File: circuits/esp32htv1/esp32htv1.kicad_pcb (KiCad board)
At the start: 2 copper layers, 56.6 x 57.7 mm, 8 parts, among them U1 BME280, U2 ESP32-WROOM-32UE, U3 LD1117S33TR_SOT223

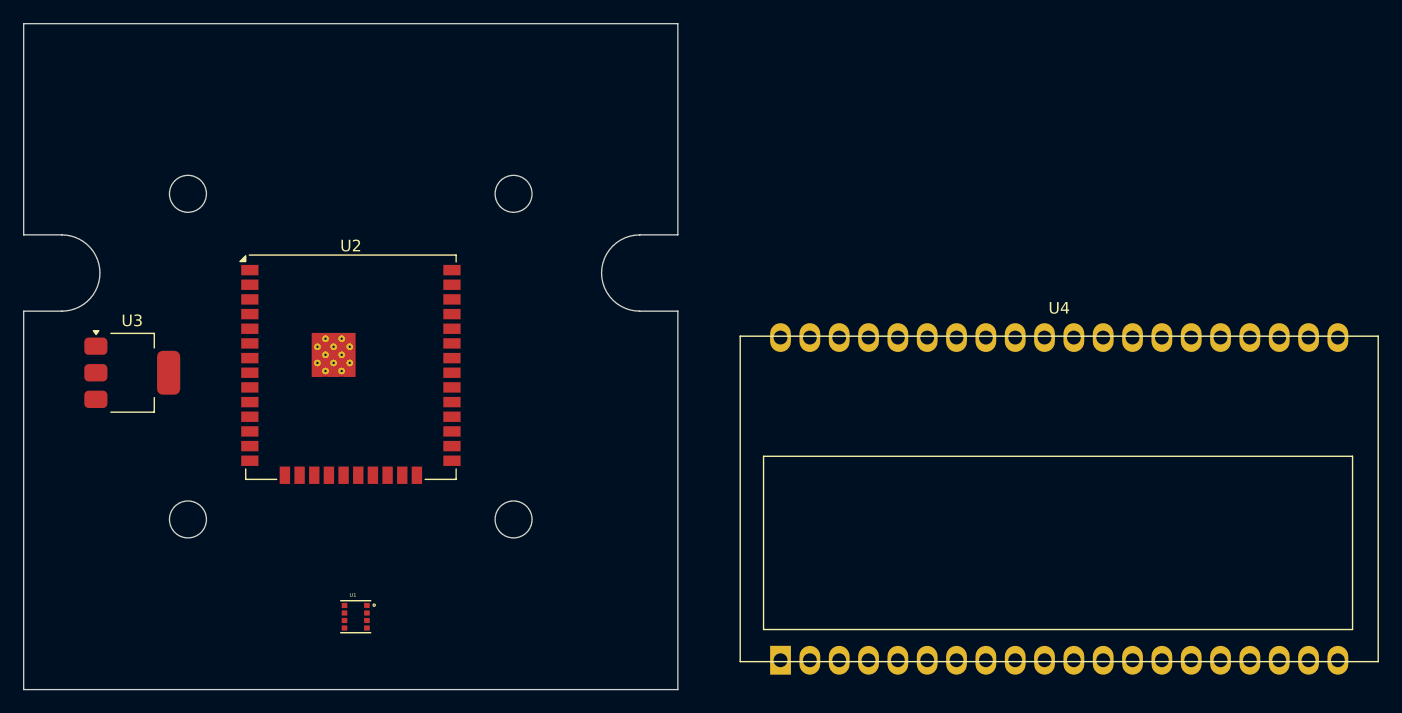
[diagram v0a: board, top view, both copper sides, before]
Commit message: Updated ESP32 HTV circuit and a prototype version (esp32htv0) of the same circuit
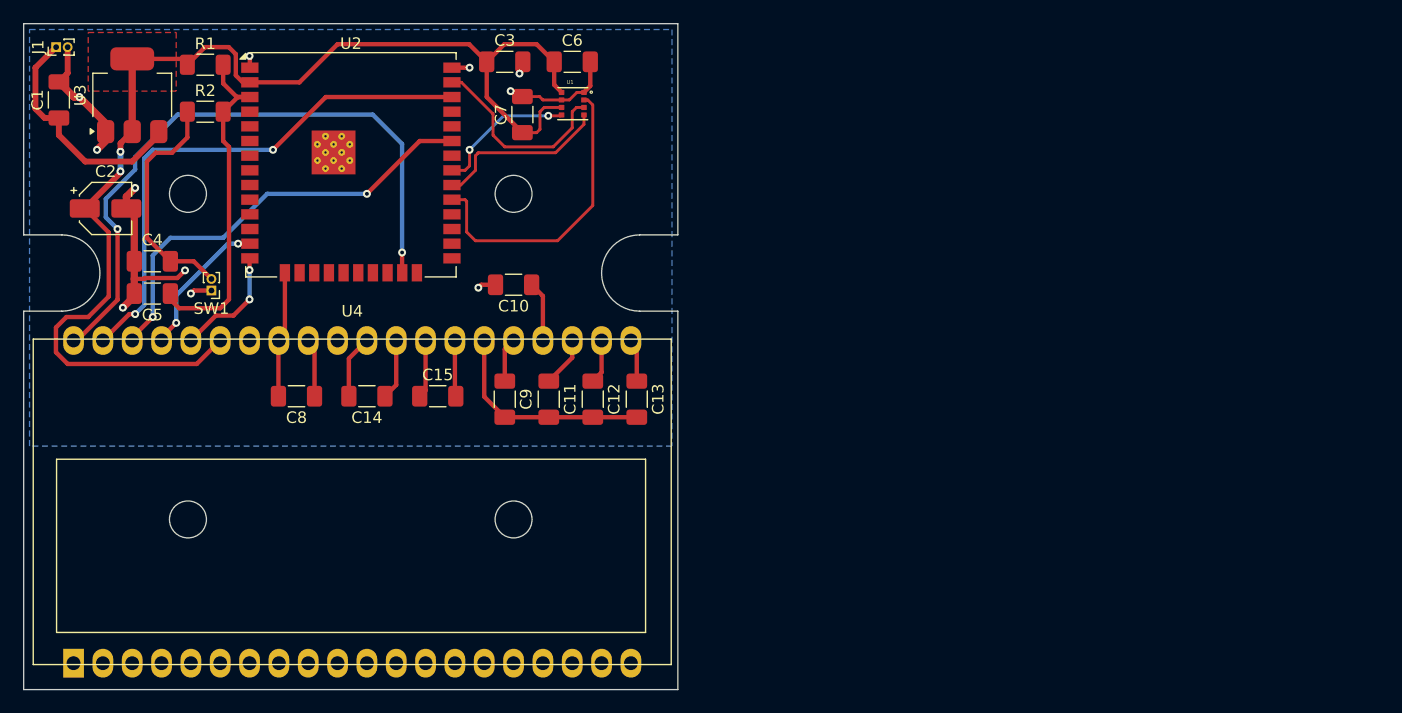
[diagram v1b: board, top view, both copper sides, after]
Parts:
- added C1: .1 uF, Capacitor_SMD:C_1206_3216Metric_Pad1.33x1.80mm_HandSolder, F.Cu at (103.0, 48.9)
- added C10: 1 uF, Capacitor_SMD:C_1206_3216Metric_Pad1.33x1.80mm_HandSolder, F.Cu at (142.4, 64.9)
- added C11: 1 uF, Capacitor_SMD:C_1206_3216Metric_Pad1.33x1.80mm_HandSolder, F.Cu at (145.5, 74.9)
- added C12: 1 uF, Capacitor_SMD:C_1206_3216Metric_Pad1.33x1.80mm_HandSolder, F.Cu at (149.3, 74.9)
- added C13: 1 uF, Capacitor_SMD:C_1206_3216Metric_Pad1.33x1.80mm_HandSolder, F.Cu at (153.1, 74.9)
- added C14: 1 uF, Capacitor_SMD:C_1206_3216Metric_Pad1.33x1.80mm_HandSolder, F.Cu at (129.7, 74.6)
- added C15: 1 uF, Capacitor_SMD:C_1206_3216Metric_Pad1.33x1.80mm_HandSolder, F.Cu at (135.9, 74.6)
- added C2: 22 uF, Capacitor_SMD:CP_Elec_4x5.4, F.Cu at (107.1, 58.3)
- added C3: 100 nF, Capacitor_SMD:C_1206_3216Metric_Pad1.33x1.80mm_HandSolder, F.Cu at (141.7, 45.6)
- added C4: 100 nF, Capacitor_SMD:C_1206_3216Metric_Pad1.33x1.80mm_HandSolder, F.Cu at (111.1, 62.9)
- added C5: 1 uF, Capacitor_SMD:C_1206_3216Metric_Pad1.33x1.80mm_HandSolder, F.Cu at (111.1, 65.7)
- added C6: 100 nF, Capacitor_SMD:C_1206_3216Metric_Pad1.33x1.80mm_HandSolder, F.Cu at (147.5, 45.6)
- added C7: 100 nF, Capacitor_SMD:C_1206_3216Metric_Pad1.33x1.80mm_HandSolder, F.Cu at (143.2, 50.2)
- added C8: 1 uF, Capacitor_SMD:C_1206_3216Metric_Pad1.33x1.80mm_HandSolder, F.Cu at (123.6, 74.6)
- added C9: 1 uF, Capacitor_SMD:C_1206_3216Metric_Pad1.33x1.80mm_HandSolder, F.Cu at (141.7, 74.9)
- added J1: Power, Connector_PinHeader_1.00mm:PinHeader_1x02_P1.00mm_Vertical, F.Cu at (102.8, 44.4)
- added R1: 10k, Resistor_SMD:R_1206_3216Metric_Pad1.30x1.75mm_HandSolder, F.Cu at (115.7, 45.9)
- added R2: 10, Resistor_SMD:R_1206_3216Metric_Pad1.30x1.75mm_HandSolder, F.Cu at (115.7, 50.0)
- added SW1: SW_Push, Connector_PinHeader_1.00mm:PinHeader_1x02_P1.00mm_Vertical, F.Cu at (116.3, 65.4)
- moved U4 61.2 mm to (128.4, 87.6)
- moved U1 48.2 mm to (147.5, 49.3)
- moved U3 24.0 mm to (109.4, 48.5), turned to 90 degrees
- moved U2 17.5 mm to (128.3, 54.6)
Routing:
- net +3V3: track 0.00 -> 104.9 mm, vias 0 -> 2
- net GND: track 0.00 -> 74.2 mm, vias 0 -> 11
- net Net-(U2-IO15): track 0.00 -> 56.0 mm, vias 0 -> 2
- net Net-(U2-IO22): track 0.00 -> 46.4 mm, vias 0 -> 2
- net Net-(U2-IO21): track 0.00 -> 38.1 mm, vias 0 -> 2
- net Net-(U2-EN): track 0.00 -> 29.9 mm
- net Net-(U1-CSB): track 0.00 -> 26.1 mm
- net +5V: track 0.00 -> 20.8 mm
- net Net-(C4-Pad2): track 0.00 -> 20.3 mm
- net Net-(U1-SDI): track 0.00 -> 17.1 mm
- net Net-(U1-SCK): track 0.00 -> 15.2 mm
- net Net-(U2-IO14): track 0.00 -> 12.7 mm, vias 0 -> 2
- net Net-(U1-SDO): track 0.00 -> 12.3 mm, vias 0 -> 2
- net Net-(U2-IO12): track 0.00 -> 10.1 mm, vias 0 -> 2
- net Net-(U4-CAP1N): track 0.00 -> 5.47 mm
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- added copper zone on F.Cu, net +3V3
- added copper zone on B.Cu, net GND

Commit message: Second version of the ESP32 HTV project
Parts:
- removed C11, C12, C13, C14, C15: 1 uF, Capacitor_SMD:C_1206_3216Metric_Pad1.33x1.80mm_HandSolder
- added J2: UART, Connector_PinHeader_2.54mm:PinHeader_1x04_P2.54mm_Vertical, F.Cu at (153.8, 47.7)
- added SW2: BOOT, Connector_PinSocket_2.54mm:PinSocket_1x02_P2.54mm_Vertical, F.Cu at (152.6, 73.3)
- J1, SW1: footprint Connector_PinHeader_1.00mm:PinHeader_1x02_P1.00mm_Vertical -> Connector_PinSocket_2.54mm:PinSocket_1x02_P2.54mm_Vertical
- U4: footprint gos:DOGM132-5 -> gos:DOGS102-6
- moved C6 49.8 mm to (145.2, 95.4), turned to 90 degrees
- moved U1 45.5 mm to (149.8, 94.7)
- moved R2 40.8 mm to (131.0, 87.8), turned to 180 degrees
- moved C7 40.7 mm to (151.3, 90.1), turned to 0 degrees
- moved C4 36.4 mm to (130.9, 93.4)
- moved SW1 34.3 mm to (129.7, 97.0), turned to 90 degrees
- moved C9 30.6 mm to (138.6, 44.4), turned to 180 degrees
- moved C8 30.4 mm to (138.6, 48.2)
- moved J1 28.3 mm to (104.6, 72.6), turned to 0 degrees
- moved C5 25.9 mm to (124.6, 87.8)
- moved C2 23.3 mm to (104.6, 81.5), turned to 90 degrees
- moved C1 22.7 mm to (108.4, 71.0), turned to -90 degrees
- moved C3 22.0 mm to (123.4, 57.8), turned to 90 degrees
- moved U3 19.2 mm to (114.2, 67.1)
- moved C10 17.5 mm to (146.5, 47.9), turned to 0 degrees
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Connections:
- C10 pad 1: Net-(U4-V3) -> Net-(U4-VLCD)
- C8 pad 1: Net-(U4-CAP3P) -> Net-(U4-VB0-)
- C8 pad 2: GND -> Net-(U4-VB0+)
- C9 pad 1: Net-(U4-V4) -> Net-(U4-VB1-)
- C9 pad 2: GND -> Net-(U4-VB1+)
- U2 pad 14: Net-(U2-IO12) -> unconnected-(U2-IO12-Pad14)
- U2 pad 16: unconnected-(U2-IO13-Pad16) -> Net-(U2-IO13)
- U2 pad 25: unconnected-(U2-IO0-Pad25) -> Net-(U2-IO0)
- U2 pad 27: unconnected-(U2-IO16-Pad27) -> Net-(U2-IO16)
- U2 pad 28: unconnected-(U2-IO17-Pad28) -> Net-(U2-IO17)
- U2 pad 33: Net-(U2-IO21) -> unconnected-(U2-IO21-Pad33)
- U2 pad 34: unconnected-(U2-RXD0/IO3-Pad34) -> Net-(J2-Pin_3)
- U2 pad 35: unconnected-(U2-TXD0/IO1-Pad35) -> Net-(J2-Pin_2)
- U2 pad 36: Net-(U2-IO22) -> unconnected-(U2-IO22-Pad36)
- U4 pad 15: (no net) -> Net-(U4-VLCD)
- U4 pad 16: (no net) -> Net-(U4-VB1-)
- U4 pad 17: (no net) -> Net-(U4-VB0-)
- U4 pad 18: (no net) -> Net-(U4-VB0+)
- U4 pad 19: (no net) -> Net-(U4-VB1+)
- U4 pad 20: (no net) -> GND
- U4 pad 21: Net-(U4-V0) -> GND
- U4 pad 22: Net-(U4-V1) -> +3V3
- U4 pad 23: Net-(U4-V2) -> +3V3
- U4 pad 24: Net-(U4-V3) -> Net-(U2-IO13)
- U4 pad 25: Net-(U4-V4) -> Net-(U2-IO14)
- U4 pad 26: GND -> Net-(U2-IO16)
- U4 pad 27: Net-(U4-CAP2N) -> Net-(U2-IO17)
- U4 pad 28: Net-(U4-CAP2P) -> Net-(U2-IO15)
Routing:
- net +3V3: track 104.9 -> 202.3 mm, vias 2 -> 7
- net GND: track 74.2 -> 8.59 mm, vias 11 -> 27
- net Net-(U2-IO17): track 0.00 -> 52.2 mm
- net Net-(U2-IO16): track 0.00 -> 48.6 mm
- net Net-(U2-IO22): track 46.4 -> 0.00 mm, vias 2 -> 0
- net Net-(U2-IO21): track 38.1 -> 0.00 mm, vias 2 -> 0
- net Net-(U2-IO13): track 0.00 -> 33.7 mm
- net Net-(U1-SDO): track 12.3 -> 38.1 mm
- net Net-(J2-Pin_2): track 0.00 -> 22.1 mm, vias 0 -> 2
- net Net-(U1-SDI): track 17.1 -> 38.5 mm
- net Net-(J2-Pin_3): track 0.00 -> 21.0 mm, vias 0 -> 2
- net Net-(U1-SCK): track 15.2 -> 32.7 mm, vias 0 -> 2
- net Net-(U2-IO14): track 12.7 -> 28.8 mm, vias 2 -> 0
- net Net-(U2-IO0): track 0.00 -> 13.1 mm, vias 0 -> 2
- net Net-(C4-Pad2): track 20.3 -> 9.25 mm
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- added copper zone on F.Cu, net GND
